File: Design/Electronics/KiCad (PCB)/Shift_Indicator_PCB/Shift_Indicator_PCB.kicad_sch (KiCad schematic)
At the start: 11 parts, among them J1 LIN Bus (K-Line), J2 Arduino Pin 8, J3 Arduino Pin 11, J4 Arduino Pin 9

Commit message: add LED display on schematic
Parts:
- added D3: Green LED 1, symbol Device:LED
- added D4: Green LED 2, symbol Device:LED
- added D5: Green LED 3, symbol Device:LED
- added D6: Yellow LED 1, symbol Device:LED
- added D7: Yellow LED 2, symbol Device:LED
- added D8: Red LED 1, symbol Device:LED
- added D9: Red LED 2, symbol Device:LED
- added J10: Arduino Pin 4, symbol Connector:Conn_01x01_Pin
- added J11: Arduino Pin 3, symbol Connector:Conn_01x01_Pin
- added J12: Arduino Pin 2, symbol Connector:Conn_01x01_Pin
- added J5: Arduino GND, symbol Connector:Conn_01x01_Pin
- added J6: Arduino Pin 12, symbol Connector:Conn_01x01_Pin
- added J7: Arduino Pin 7, symbol Connector:Conn_01x01_Pin
- added J8: Arduino Pin 6, symbol Connector:Conn_01x01_Pin
- added J9: Arduino Pin 5, symbol Connector:Conn_01x01_Pin
- added R3, R4, R5, R6, R7, R8, R9: 220Ω, symbol Device:R
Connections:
- net GND: now also D3.1 (K), D4.1 (K), D5.1 (K), D6.1 (K), D7.1 (K), D8.1 (K), D9.1 (K), J5.1 (Pin_1)
- new net: D7.2 (A), R7.1
- new net: D5.2 (A), R5.1
- new net: J8.1 (Pin_1), R5.2
- new net: J6.1 (Pin_1), R3.2
- new net: J11.1 (Pin_1), R8.2
- new net: D4.2 (A), R4.1
- new net: J7.1 (Pin_1), R4.2
- new net: J9.1 (Pin_1), R6.2
- new net: D6.2 (A), R6.1
- new net: J12.1 (Pin_1), R9.2
- new net: D8.2 (A), R8.1
- new net: D9.2 (A), R9.1
- new net: D3.2 (A), R3.1
- new net: J10.1 (Pin_1), R7.2

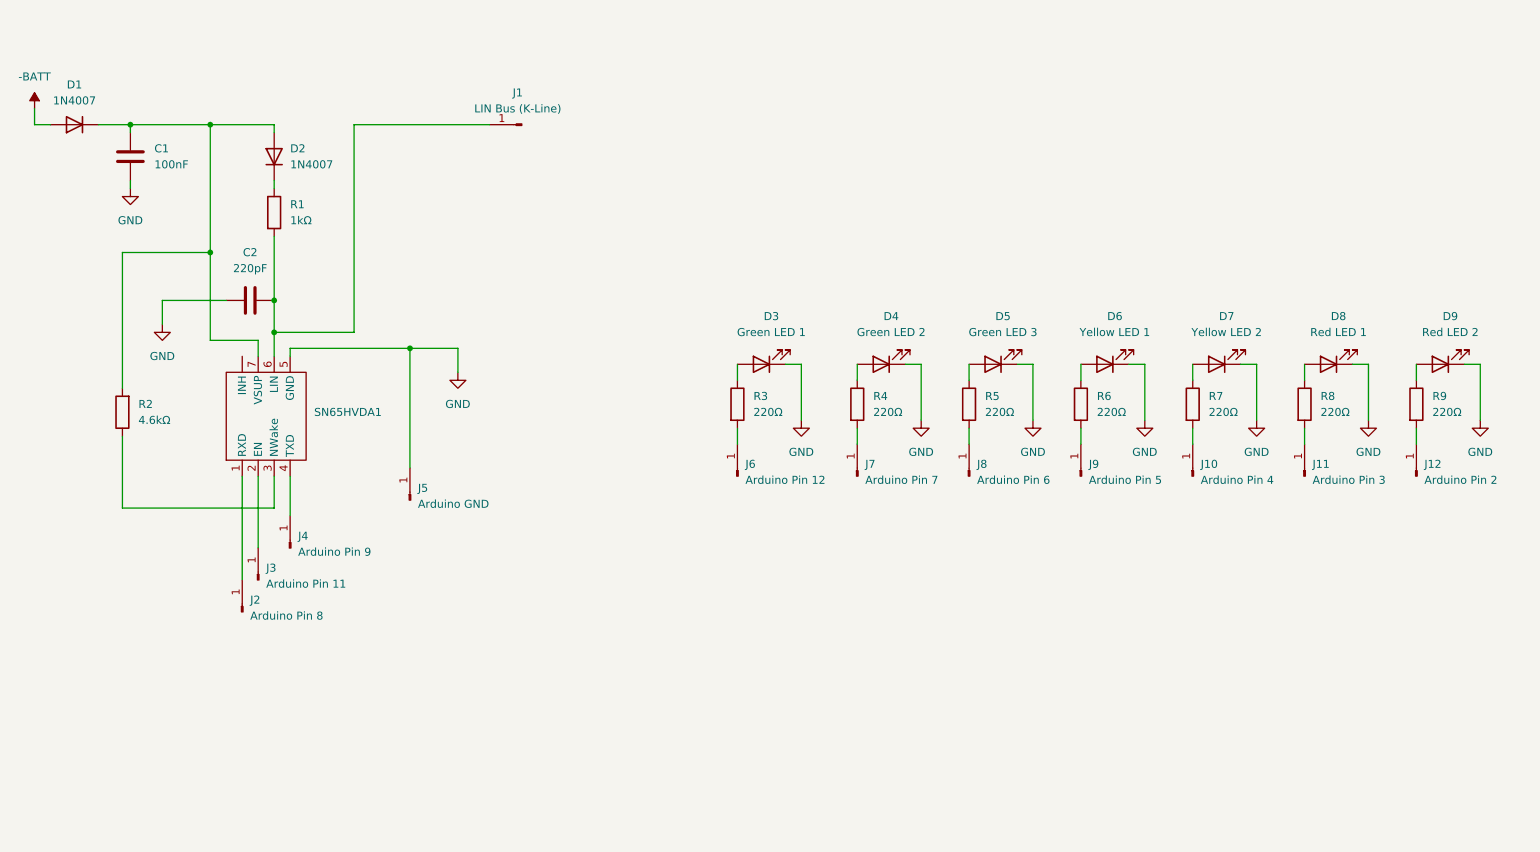
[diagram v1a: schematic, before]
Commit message: schematic: added proper connectors for OBDII and Arduino
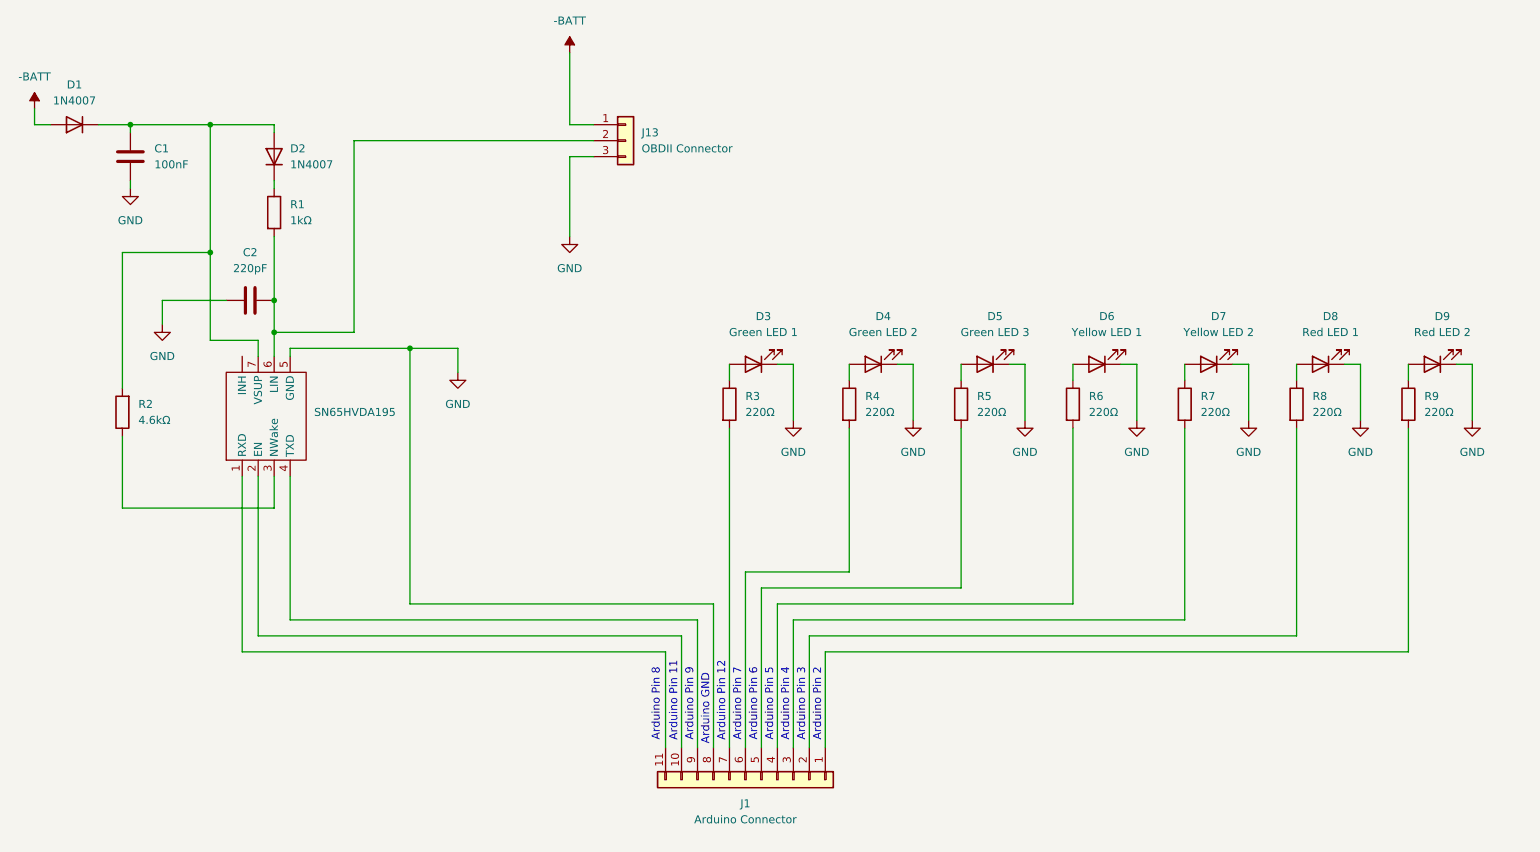
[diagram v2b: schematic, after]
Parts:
- removed J1: LIN Bus (K-Line), symbol Connector:Conn_01x01_Pin
- removed J10: Arduino Pin 4, symbol Connector:Conn_01x01_Pin
- removed J11: Arduino Pin 3, symbol Connector:Conn_01x01_Pin
- removed J12: Arduino Pin 2, symbol Connector:Conn_01x01_Pin
- removed J2: Arduino Pin 8, symbol Connector:Conn_01x01_Pin
- removed J3: Arduino Pin 11, symbol Connector:Conn_01x01_Pin
- removed J4: Arduino Pin 9, symbol Connector:Conn_01x01_Pin
- removed J5: Arduino GND, symbol Connector:Conn_01x01_Pin
- removed J6: Arduino Pin 12, symbol Connector:Conn_01x01_Pin
- removed J7: Arduino Pin 7, symbol Connector:Conn_01x01_Pin
- removed J8: Arduino Pin 6, symbol Connector:Conn_01x01_Pin
- removed J9: Arduino Pin 5, symbol Connector:Conn_01x01_Pin
- added J1: Arduino Connector, symbol Connector_Generic:Conn_01x11
- added J13: OBDII Connector, symbol Connector_Generic:Conn_01x03
- C1, C2: footprint (none) -> Capacitor_SMD:C_0603_1608Metric_Pad1.08x0.95mm_HandSolder
- D3, D4, D5, D6, D7, D8, D9: footprint (none) -> LED_SMD:LED_0603_1608Metric_Pad1.05x0.95mm_HandSolder
- R1, R2, R3, R4, R5, R6, R7, R8, R9: footprint (none) -> Resistor_SMD:R_0603_1608Metric_Pad0.98x0.95mm_HandSolder
- SN65HVDA195: renamed from SN65HVDA1; footprint (none) -> Package_SO:SOIC-8_3.9x4.9mm_P1.27mm
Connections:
- net -BATT: now also J13.1 (Pin_1)
- net GND: now also J1.8 (Pin_8), J13.3 (Pin_3)
- net at R5.2: now also J1.5 (Pin_5)
- net at R3.2: now also J1.7 (Pin_7)
- net at R8.2: now also J1.2 (Pin_2)
- net at R4.2: now also J1.6 (Pin_6)
- net at R6.2: now also J1.4 (Pin_4)
- net at R9.2: now also J1.1 (Pin_1)
- net at SN65HVDA195.1 (RXD): now also J1.11 (Pin_11)
- net at SN65HVDA195.2 (EN): now also J1.10 (Pin_10)
- net at SN65HVDA195.4 (TXD): now also J1.9 (Pin_9)
- net at C2.2, R1.2, SN65HVDA195.6 (LIN): now also J13.2 (Pin_2)
- net at R7.2: now also J1.3 (Pin_3)
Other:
- note added: "Arduino GND"
- note added: "Arduino Pin 11"
- note added: "Arduino Pin 12"
- note added: "Arduino Pin 2"
- note added: "Arduino Pin 3"
- note added: "Arduino Pin 4"
- note added: "Arduino Pin 5"
- note added: "Arduino Pin 6"
- note added: "Arduino Pin 7"
- note added: "Arduino Pin 8"
- note added: "Arduino Pin 9"
- moved on the sheet: D3, D4, D5, D6, D7, D8, D9, R3, R4, R5, R6, R7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

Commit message: added first iteration of PCB
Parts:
- added F1: Fuse (200mA), Fuse:Fuseholder_Cylinder-5x20mm_Stelvio-Kontek_PTF78_Horizontal_Open, symbol Device:Fuse
- added H1, H2, H3, H4: MountingHole, MountingHole:MountingHole_3.2mm_M3_Pad, symbol Mechanical:MountingHole
- added J2: GND, Connector_PinHeader_2.54mm:PinHeader_1x01_P2.54mm_Vertical, symbol Connector_Generic:Conn_01x01
- added J3: Batt, Connector_PinHeader_2.54mm:PinHeader_1x01_P2.54mm_Vertical, symbol Connector_Generic:Conn_01x01
- added J4: LIN, Connector_PinHeader_2.54mm:PinHeader_1x01_P2.54mm_Vertical, symbol Connector_Generic:Conn_01x01
- C1, C2: footprint Capacitor_SMD:C_0603_1608Metric_Pad1.08x0.95mm_HandSolder -> Capacitor_SMD:C_0805_2012Metric_Pad1.18x1.45mm_HandSolder
- D3, D4, D5, D6, D7, D8, D9: footprint LED_SMD:LED_0603_1608Metric_Pad1.05x0.95mm_HandSolder -> LED_THT:LED_D1.8mm_W3.3mm_H2.4mm
- J1: footprint (none) -> Connector_PinSocket_2.54mm:PinSocket_1x11_P2.54mm_Vertical
- J13: footprint (none) -> Connector_PinSocket_2.54mm:PinSocket_1x03_P2.54mm_Vertical
- R1, R2, R3, R4, R5, R6, R7, R8, R9: footprint Resistor_SMD:R_0603_1608Metric_Pad0.98x0.95mm_HandSolder -> Resistor_SMD:R_0805_2012Metric_Pad1.20x1.40mm_HandSolder
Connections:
- net -BATT: now also F1.1; no longer J13.1 (Pin_1)
- net GND: now also J2.1 (Pin_1)
- net at C2.2, J13.2 (Pin_2), R1.2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: now also J4.1 (Pin_1)
- new net: F1.2, J13.1 (Pin_1), J3.1 (Pin_1)
- no-connect marks 0 -> 1

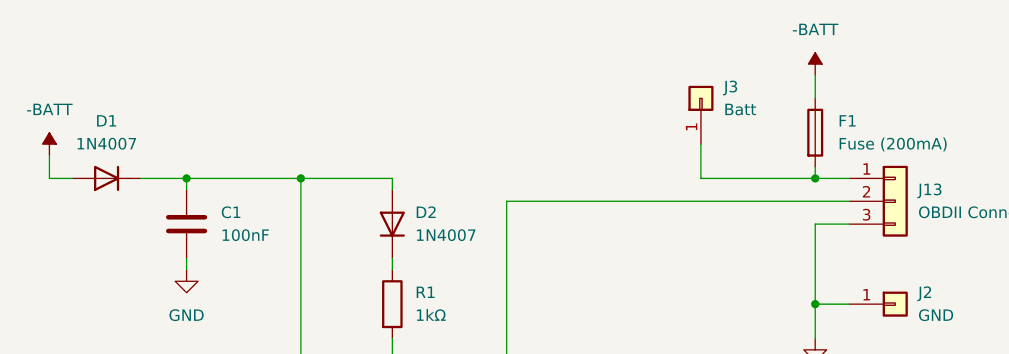
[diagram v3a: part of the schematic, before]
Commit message: fix PCB for approval + netlist/BOM
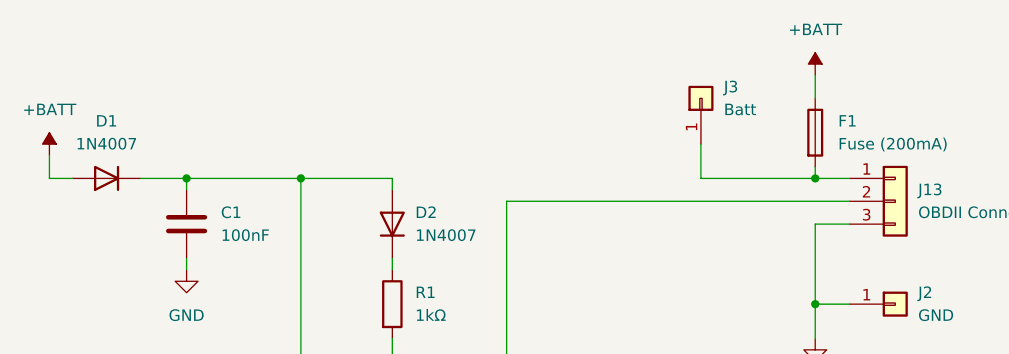
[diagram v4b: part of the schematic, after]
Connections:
- net -BATT renamed +BATT
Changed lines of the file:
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@@
 			)
 		)
-		(property "Value" "-BATT"
+		(property "Value" "+BATT"
 			(at 118.11 21.59 0)
 			(effects
@@
 			)
 		)
-		(property "Value" "-BATT"
+		(property "Value" "+BATT"
 			(at 33.02 30.48 0)
 			(effects

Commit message: add all DigiKey part numbers to BOM
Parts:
- C1: Part Number (none) -> 0805B104K101CC
- C2: Part Number (none) -> 0805B221K500BD
- D1, D2: Part Number (none) -> 1N4007-T
- D3, D4, D5: Part Number (none) -> LTL-709L
- D6, D7: Part Number (none) -> LTL-709Y
- D8, D9: Part Number (none) -> LTL-709E
- F1: Part Number (none) -> F6094-ND & 0235.200HXP
- J1: Part Number (none) -> PPTC111LFBN-RC
- J13: Part Number (none) -> PPPC031LFBN-RC
- J2, J3, J4: Part Number (none) -> PH1-01-UA
- R1: Part Number (none) -> RC0805FR-071KL
- R2: Part Number (none) -> ERJ-6ENF4991V
- R3, R4, R5, R6, R7, R8, R9: Part Number (none) -> CRGCQ0805F220R
- SN65HVDA195: Part Number (none) -> SN65HVDA195QDRQ1
